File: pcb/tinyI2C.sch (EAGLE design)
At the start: 34 parts, among them IC1 74LVC1G125DCK, IC2 74LVC1G125DCK, IC3 IC_LDO_MIC5355, U1 LPC824M201JHI33, X1 TSW-112-02-S-S, X2 TSW-112-02-S-S, X3 TSW-106-02-S-S-RA, X4 TSW-102-02-S-S, X5 TSW-102-02-S-S, X6 TSW-102-02-S-S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

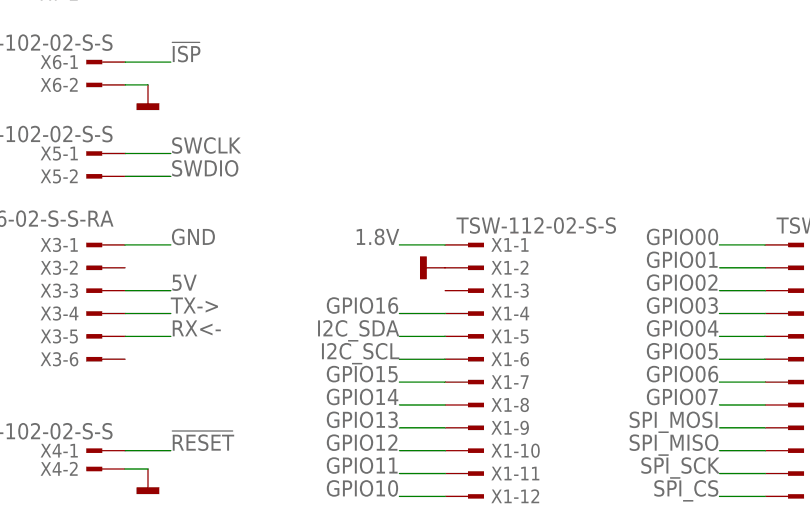
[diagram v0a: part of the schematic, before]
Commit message: [ PCB ][ SCH ] X1[3] is now Vin(5V) [ BRD ] related tracechange
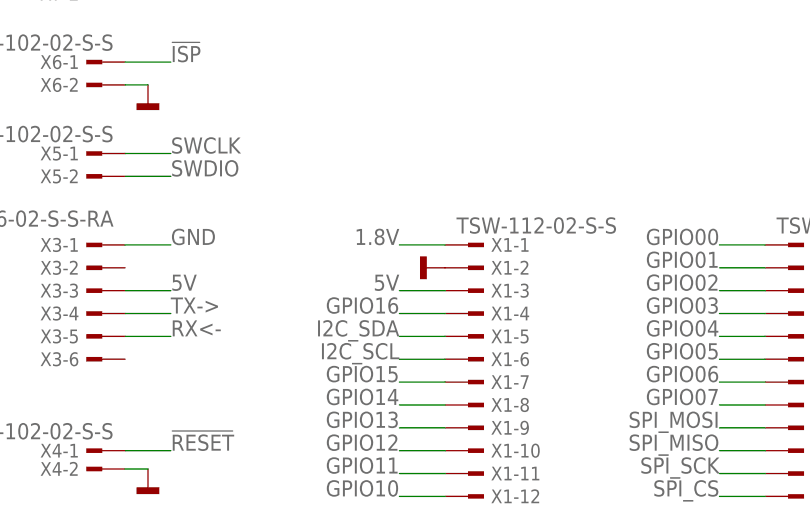
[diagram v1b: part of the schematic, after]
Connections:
- net 5V: now also X1-3.1
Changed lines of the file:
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@@
 <setting verticaltext="up"/>
 </settings>
-<grid distance="0.1" unitdist="inch" unit="inch" style="lines" multiple="1" display="no" altdistance="0.05" altunitdist="inch" altunit="inch"/>
+<grid distance="0.1" unitdist="inch" unit="inch" style="lines" multiple="1" display="no" altdistance="0.01" altunitdist="inch" altunit="inch"/>
 <layers>
 <layer number="1" name="Top" color="4" fill="1" visible="no" active="no"/>
@@
 <pinref part="IC3" gate="G$1" pin="EN1"/>
 </segment>
+<segment>
+<wire x1="68.58" y1="35.56" x2="63.5" y2="35.56" width="0.1524" layer="91"/>
+<label x="63.5" y="35.56" size="1.778" layer="95" rot="MR0"/>
+<pinref part="X1" gate="-3" pin="1"/>
+</segment>
 </net>

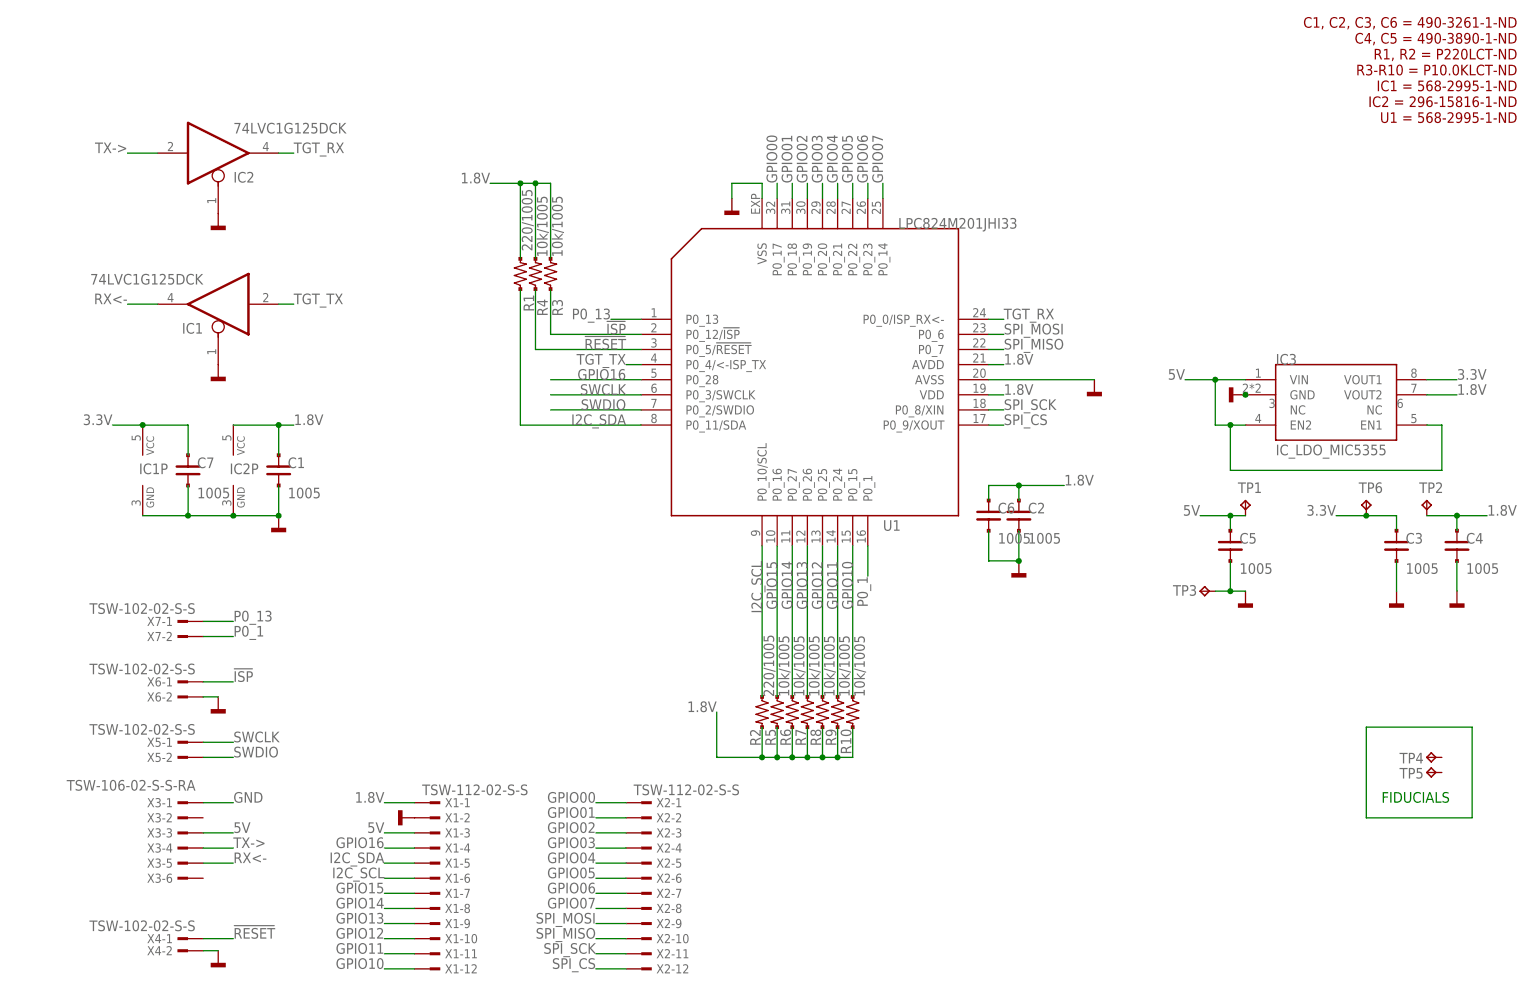
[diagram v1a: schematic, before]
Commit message: [ PCB ][ SCH ] library update related fix and move
IC3 symbol updated; fixed schematic
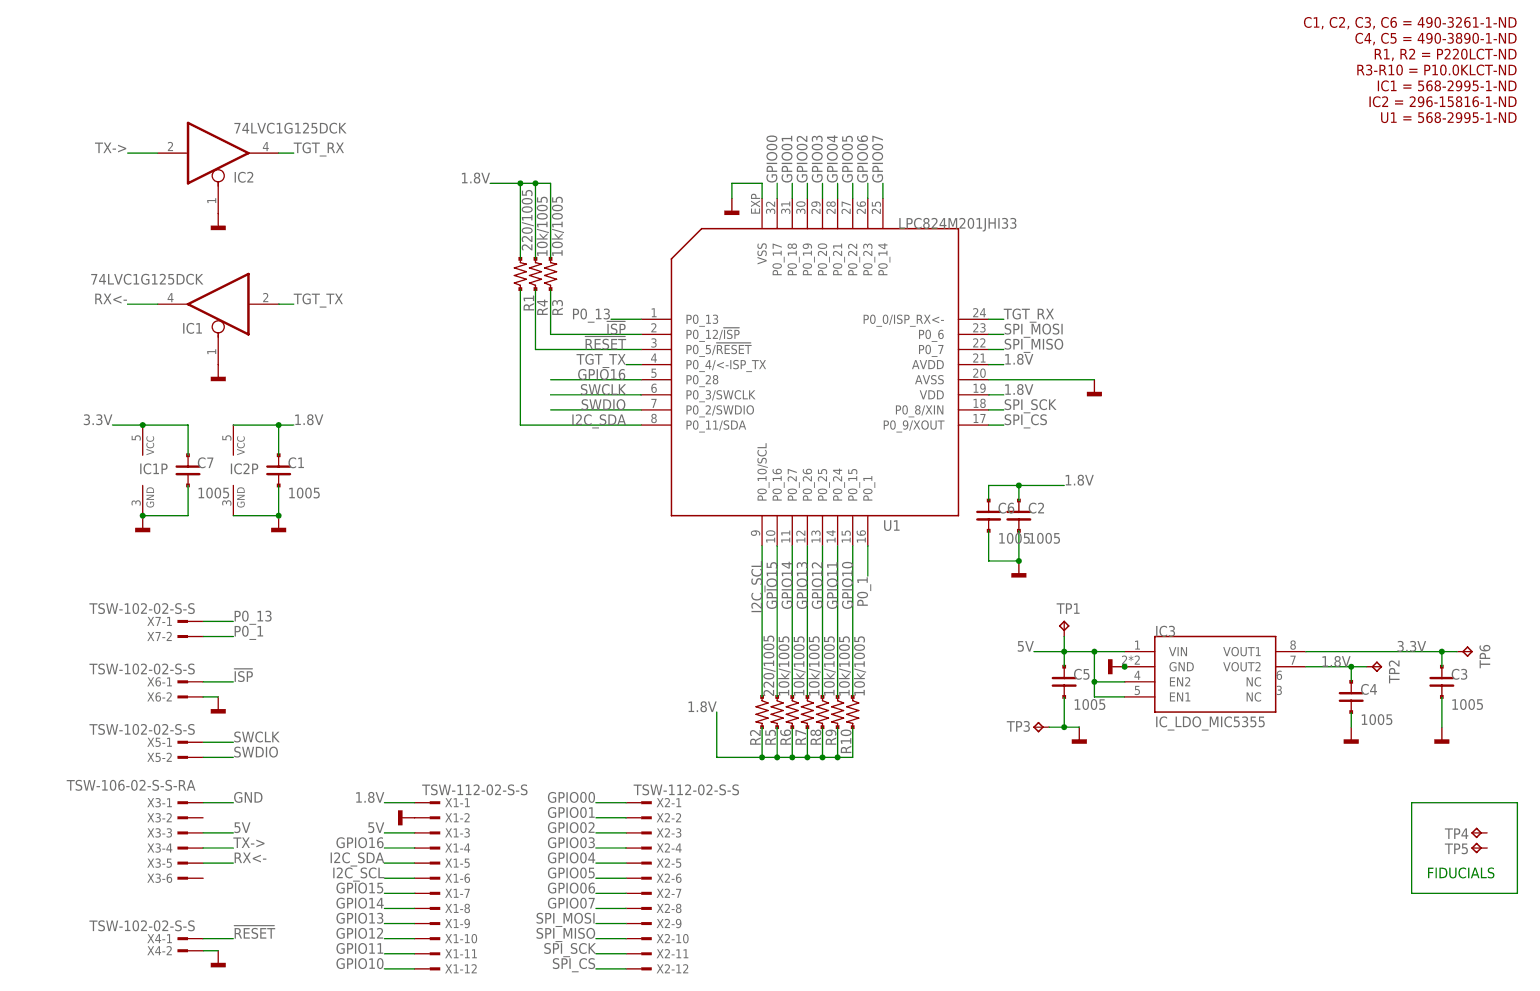
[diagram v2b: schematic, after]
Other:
- moved on the sheet: C3, C4, C5, IC3, TP1, TP2, TP3, TP4, TP5, TP6

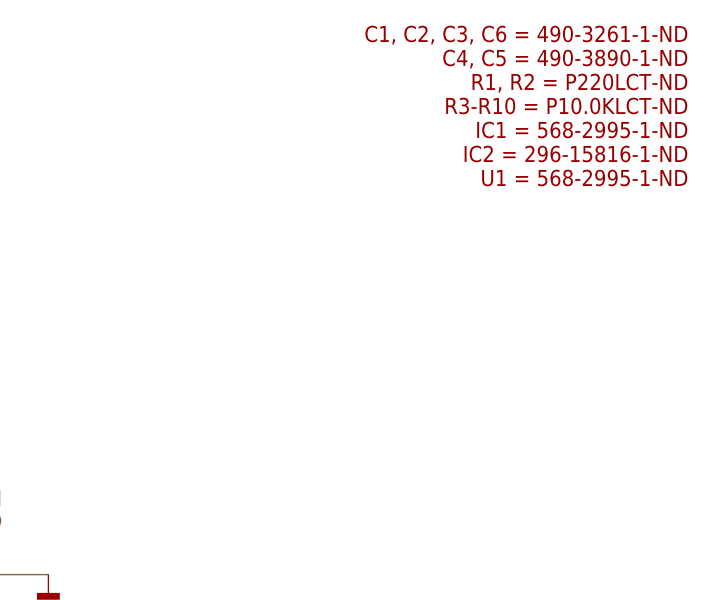
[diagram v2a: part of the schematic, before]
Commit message: [ PCB ][ SCH ] BOM update
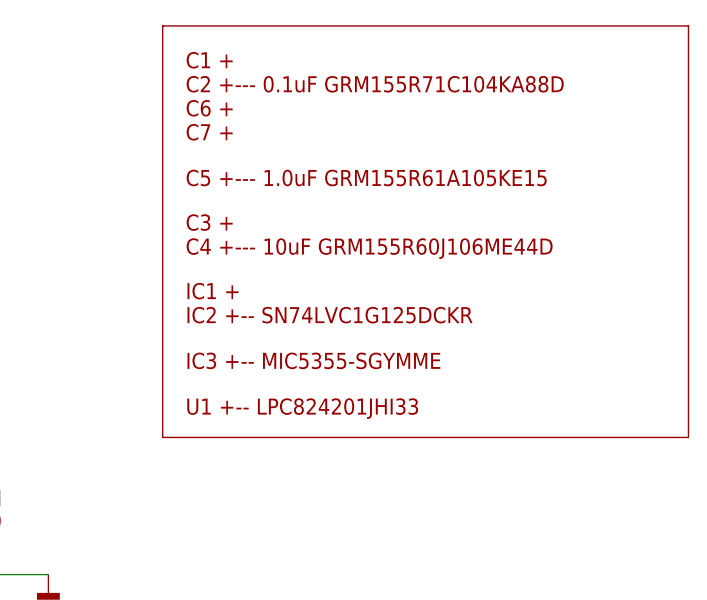
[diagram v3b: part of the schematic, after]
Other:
- note added: "C1 + C2 +--- 0.1uF GRM155R71C104KA88D C6 + C7 +"
- note added: "C3 + C4 +--- 10uF GRM155R60J106ME44D"
- note added: "C5 +--- 1.0uF GRM155R61A105KE15"
- note added: "IC1 + IC2 +-- SN74LVC1G125DCKR"
- note added: "IC3 +-- MIC5355-SGYMME"
- note added: "U1 +-- LPC824201JHI33"
- note removed: "C1, C2, C3, C6 = 490-3261-1-ND C4, C5 = 490-3890-1-ND R1, R2 = P220LCT-ND R3-R10 = P10.0KLCT-ND IC1 = 568-2995-1-ND IC2 = 296-15816-1-ND U1 = 568-2995-1-ND"
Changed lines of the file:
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@@
 <plain>
 <text x="238.76" y="27.94" size="1.778" layer="91">FIDUCIALS</text>
-<text x="254" y="172.72" size="1.778" layer="94" rot="R180">C1, C2, C3, C6 = 490-3261-1-ND
-C4, C5 = 490-3890-1-ND
-R1, R2 = P220LCT-ND
-R3-R10 = P10.0KLCT-ND
-IC1 = 568-2995-1-ND
-IC2 = 296-15816-1-ND
-U1 = 568-2995-1-ND</text>
+<text x="198.12" y="160.02" size="1.778" layer="94">C1 +
+C2 +--- 0.1uF GRM155R71C104KA88D
+C6 +
+C7 +</text>
+<wire x1="195.58" y1="172.72" x2="254" y2="172.72" width="0.1524" layer="94"/>
+<wire x1="254" y1="172.72" x2="254" y2="127" width="0.1524" layer="94"/>
+<wire x1="254" y1="127" x2="195.58" y2="127" width="0.1524" layer="94"/>
+<wire x1="195.58" y1="127" x2="195.58" y2="172.72" width="0.1524" layer="94"/>
+<text x="198.12" y="147.32" size="1.778" layer="94">C3 +
+C4 +--- 10uF GRM155R60J106ME44D</text>
+<text x="198.12" y="139.7" size="1.778" layer="94">IC1 +
+IC2 +-- SN74LVC1G125DCKR</text>
+<text x="198.12" y="134.62" size="1.778" layer="94">IC3 +-- MIC5355-SGYMME</text>
+<text x="198.12" y="154.94" size="1.778" layer="94">C5 +--- 1.0uF GRM155R61A105KE15</text>
+<text x="198.12" y="129.54" size="1.778" layer="94">U1 +-- LPC824201JHI33</text>
 </plain>
 <instances>

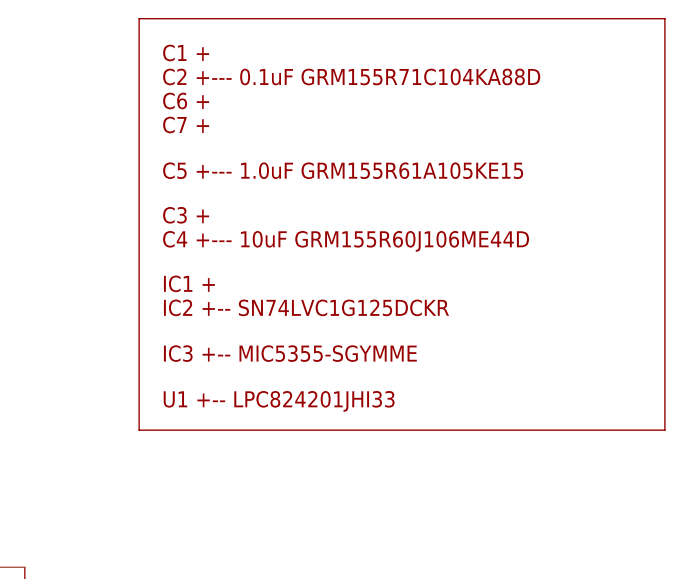
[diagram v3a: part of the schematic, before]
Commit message: [ PCB ][ SCH ] replace as library did [ BRD ] I2C / SPI silk indicator
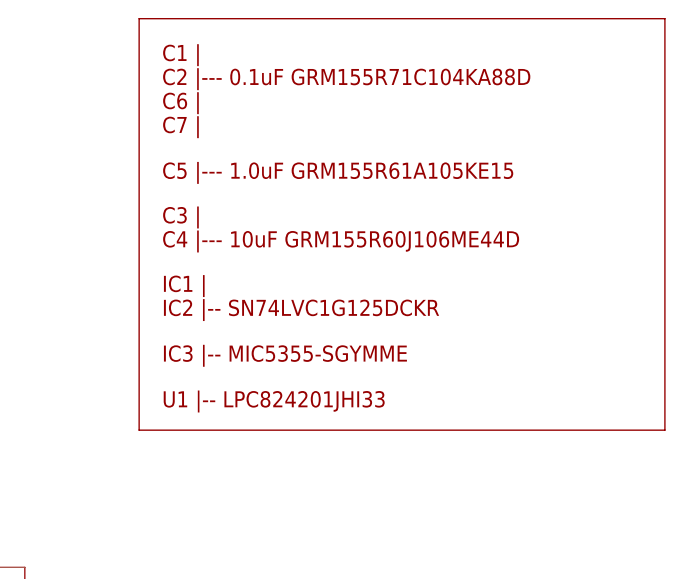
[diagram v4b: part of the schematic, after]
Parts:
- TP1, TP2, TP3, TP6: device testpad:TPTP07R -> testpad_local:TPTP07R
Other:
- note added: "C1 | C2 |--- 0.1uF GRM155R71C104KA88D C6 | C7 |"
- note added: "C3 | C4 |--- 10uF GRM155R60J106ME44D"
- note added: "C5 |--- 1.0uF GRM155R61A105KE15"
- note added: "IC1 | IC2 |-- SN74LVC1G125DCKR"
- note added: "IC3 |-- MIC5355-SGYMME"
- note added: "U1 |-- LPC824201JHI33"
- note removed: "C1 + C2 +--- 0.1uF GRM155R71C104KA88D C6 + C7 +"
- note removed: "C3 + C4 +--- 10uF GRM155R60J106ME44D"
- note removed: "C5 +--- 1.0uF GRM155R61A105KE15"
- note removed: "IC1 + IC2 +-- SN74LVC1G125DCKR"
- note removed: "IC3 +-- MIC5355-SGYMME"
- note removed: "U1 +-- LPC824201JHI33"
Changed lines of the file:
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@@
 <part name="GND10" library="mbed-HDK" deviceset="GND" device=""/>
 <part name="GND11" library="mbed-HDK" deviceset="GND" device=""/>
-<part name="TP1" library="testpad" deviceset="TP" device="TP07R"/>
-<part name="TP2" library="testpad" deviceset="TP" device="TP07R"/>
-<part name="TP3" library="testpad" deviceset="TP" device="TP07R"/>
+<part name="TP1" library="testpad_local" deviceset="TP" device="TP07R"/>
+<part name="TP2" library="testpad_local" deviceset="TP" device="TP07R"/>
+<part name="TP3" library="testpad_local" deviceset="TP" device="TP07R"/>
 <part name="R1" library="mylib" deviceset="R_US_PAD_PAD" device="_1005" value="220/1005"/>
 <part name="R2" library="mylib" deviceset="R_US_PAD_PAD" device="_1005" value="220/1005"/>
@@
 <part name="GND14" library="mbed-HDK" deviceset="GND" device=""/>
 <part name="GND15" library="mbed-HDK" deviceset="GND" device=""/>
-<part name="TP6" library="testpad" deviceset="TP" device="TP07R"/>
+<part name="TP6" library="testpad_local" deviceset="TP" device="TP07R"/>
 <part name="IC1" library="74xx-little-us_local" deviceset="74*1G125" device="DCK" technology="LVC"/>
 <part name="IC2" library="74xx-little-us_local" deviceset="74*1G125" device="DCK" technology="LVC"/>
@@
 <plain>
 <text x="238.76" y="27.94" size="1.778" layer="91">FIDUCIALS</text>
-<text x="198.12" y="160.02" size="1.778" layer="94">C1 +
-C2 +--- 0.1uF GRM155R71C104KA88D
-C6 +
-C7 +</text>
+<text x="198.12" y="160.02" size="1.778" layer="94">C1 |
+C2 |--- 0.1uF GRM155R71C104KA88D
+C6 |
+C7 |</text>
 <wire x1="195.58" y1="172.72" x2="254" y2="172.72" width="0.1524" layer="94"/>
 <wire x1="254" y1="172.72" x2="254" y2="127" width="0.1524" layer="94"/>
 <wire x1="254" y1="127" x2="195.58" y2="127" width="0.1524" layer="94"/>
 <wire x1="195.58" y1="127" x2="195.58" y2="172.72" width="0.1524" layer="94"/>
-<text x="198.12" y="147.32" size="1.778" layer="94">C3 +
-C4 +--- 10uF GRM155R60J106ME44D</text>
-<text x="198.12" y="139.7" size="1.778" layer="94">IC1 +
-IC2 +-- SN74LVC1G125DCKR</text>
-<text x="198.12" y="134.62" size="1.778" layer="94">IC3 +-- MIC5355-SGYMME</text>
-<text x="198.12" y="154.94" size="1.778" layer="94">C5 +--- 1.0uF GRM155R61A105KE15</text>
-<text x="198.12" y="129.54" size="1.778" layer="94">U1 +-- LPC824201JHI33</text>
+<text x="198.12" y="147.32" size="1.778" layer="94">C3 |
+C4 |--- 10uF GRM155R60J106ME44D</text>
+<text x="198.12" y="139.7" size="1.778" layer="94">IC1 |
+IC2 |-- SN74LVC1G125DCKR</text>
+<text x="198.12" y="134.62" size="1.778" layer="94">IC3 |-- MIC5355-SGYMME</text>
+<text x="198.12" y="154.94" size="1.778" layer="94">C5 |--- 1.0uF GRM155R61A105KE15</text>
+<text x="198.12" y="129.54" size="1.778" layer="94">U1 |-- LPC824201JHI33</text>
 </plain>
 <instances>
